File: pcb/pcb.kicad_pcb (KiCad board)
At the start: 2 copper layers, 157.6 x 114.5 mm, 33 parts, among them J1 Conn_01x10, J2 Conn_01x06, J3 Conn_01x06, J4 Conn_01x06, J5 Conn_01x06, J6 Conn_01x06, J7 Conn_01x06, J8 Conn_01x10, U1 teensy-2.0

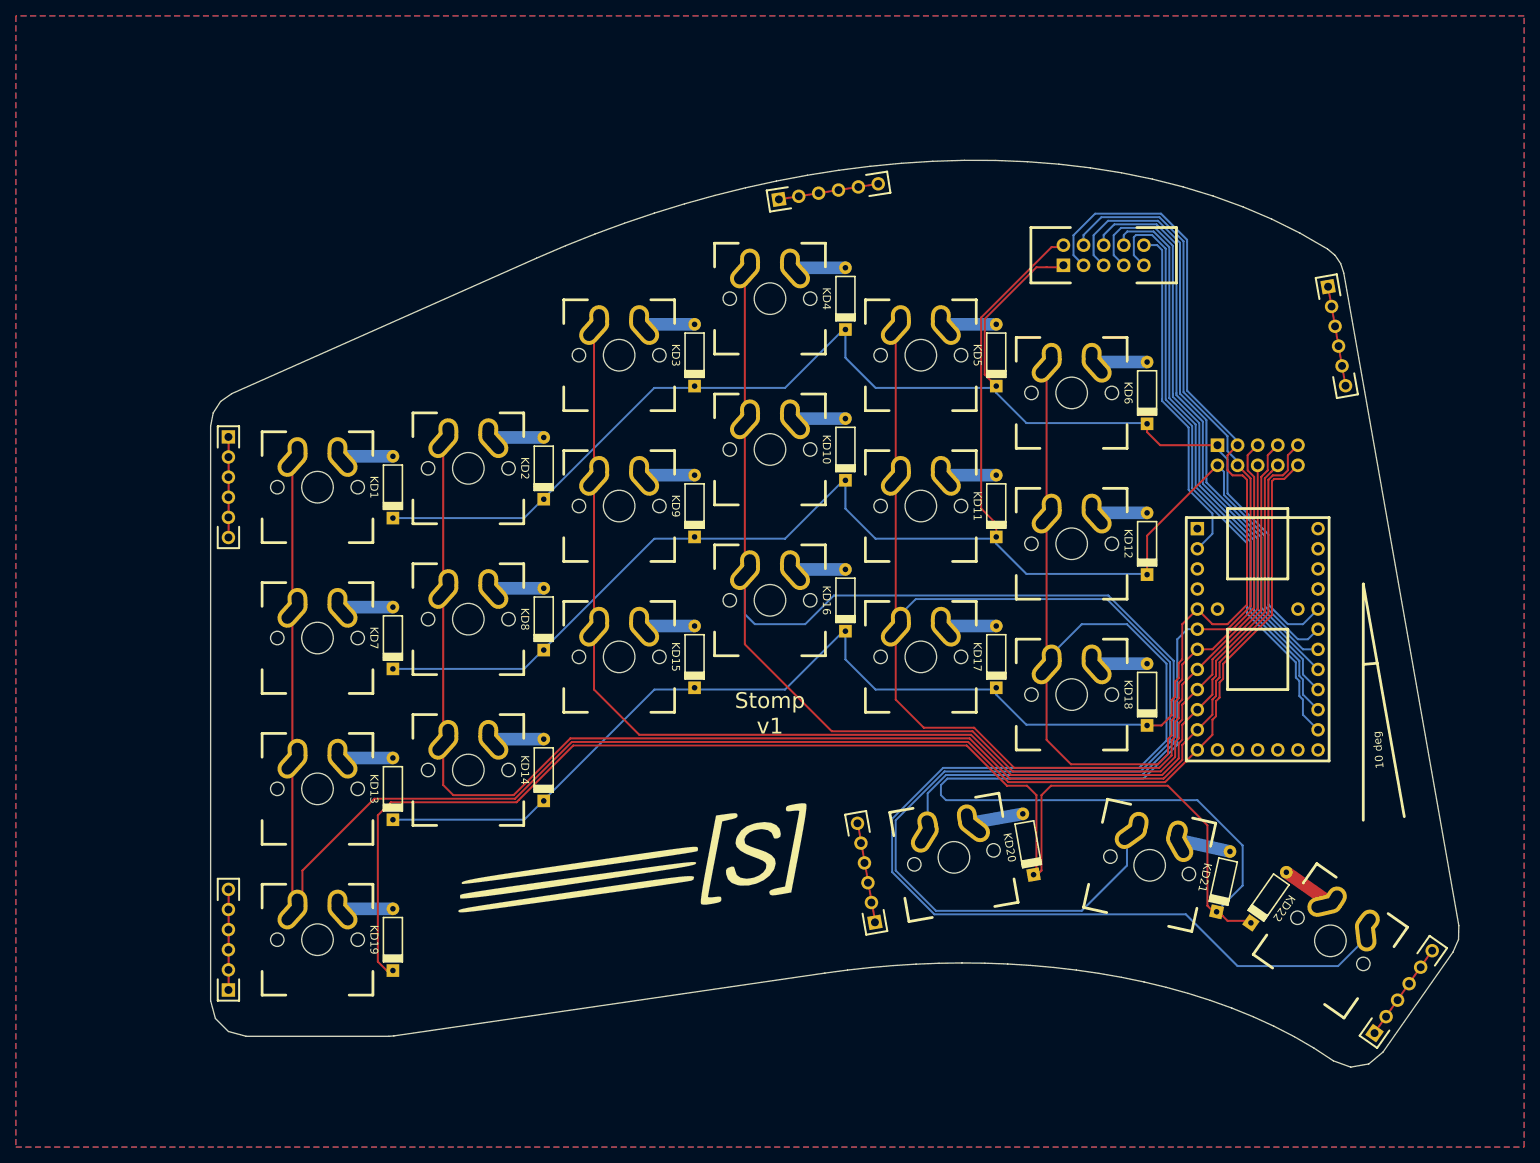
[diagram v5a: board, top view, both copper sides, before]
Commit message: Use single IDC header and prep outline for magnets
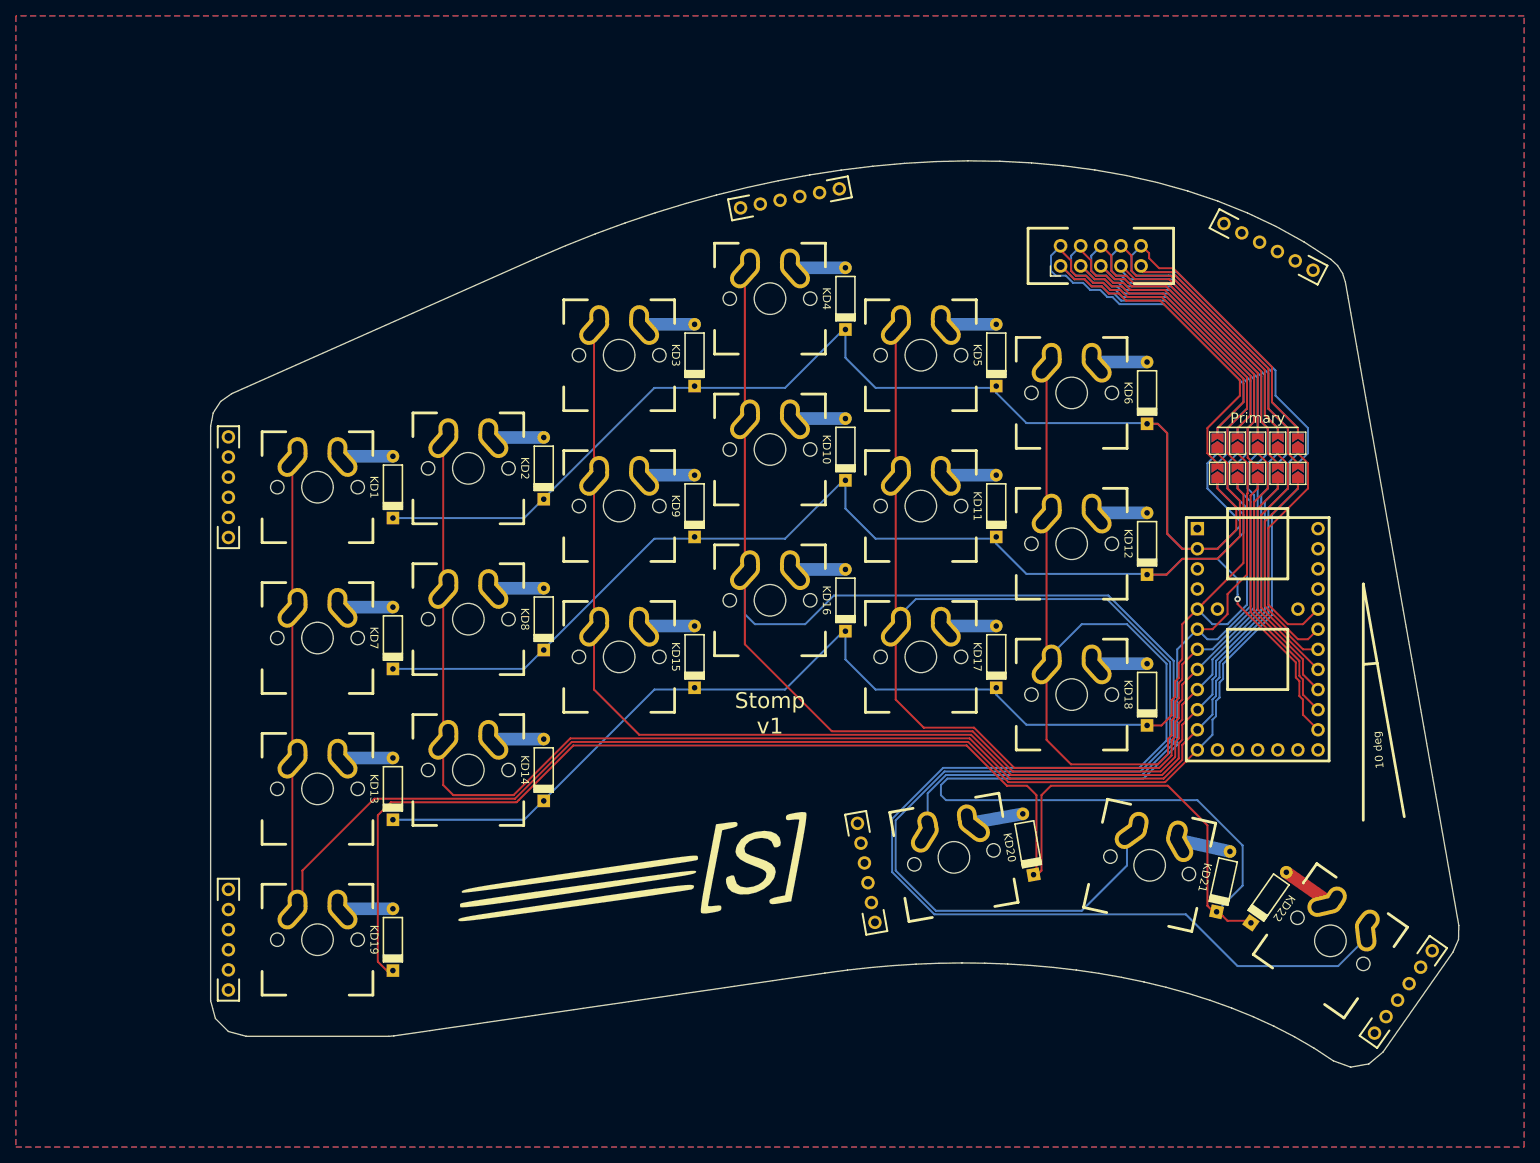
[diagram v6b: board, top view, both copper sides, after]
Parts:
- removed J8: Conn_01x10, keyboard-parts:idc-header_2x05_2.54mm
- added JP1: dualside-idc-jumpers, keyboard-parts:dualside-idc-jumpers, F.Cu at (14.0, -39.4)
- J1: footprint keyboard-parts:idc-header_2x05_2.54mm -> keyboard-parts:idc-header-dualside_2x05_2.54mm
- J2, J3, J4, J5, J6, J7: footprint keyboard-parts:header_1x06_2.54mm -> keyboard-parts:header_sym_1x06_2.54mm
- moved J2 4.96 mm to (-51.3, -71.0), turned to 100.9 degrees
- moved J7 2.82 mm to (21.0, -63.1), turned to 242.4 degrees
- moved G*** 1.11 mm to (-64.8, 13.8) (x2)
- moved J1 0.37 mm to (-5.85, -64.9)
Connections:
- J1 pad 1: /R0 -> Net-(J1-Pad1)
- J1 pad 2: /R1 -> Net-(J1-Pad2)
- J1 pad 3: /R2 -> Net-(J1-Pad3)
- J1 pad 4: /R3 -> Net-(J1-Pad4)
- J2 pad 1: Net-(J2-Pad1) -> GND
- J2 pad 2: Net-(J2-Pad1) -> GND
- J2 pad 3: Net-(J2-Pad1) -> GND
- J2 pad 4: Net-(J2-Pad1) -> GND
- J2 pad 5: Net-(J2-Pad1) -> GND
- J2 pad 6: Net-(J2-Pad1) -> GND
- J3 pad 1: Net-(J3-Pad1) -> GND
- J3 pad 2: Net-(J3-Pad1) -> GND
- J3 pad 3: Net-(J3-Pad1) -> GND
- J3 pad 4: Net-(J3-Pad1) -> GND
- J3 pad 5: Net-(J3-Pad1) -> GND
- J3 pad 6: Net-(J3-Pad1) -> GND
- J4 pad 1: Net-(J4-Pad1) -> GND
- J4 pad 2: Net-(J4-Pad1) -> GND
- J4 pad 3: Net-(J4-Pad1) -> GND
- J4 pad 4: Net-(J4-Pad1) -> GND
- J4 pad 5: Net-(J4-Pad1) -> GND
- J4 pad 6: Net-(J4-Pad1) -> GND
- J5 pad 1: Net-(J5-Pad1) -> GND
- J5 pad 2: Net-(J5-Pad1) -> GND
- J5 pad 3: Net-(J5-Pad1) -> GND
- J5 pad 4: Net-(J5-Pad1) -> GND
- J5 pad 5: Net-(J5-Pad1) -> GND
- J5 pad 6: Net-(J5-Pad1) -> GND
- J6 pad 1: Net-(J6-Pad1) -> GND
- J6 pad 2: Net-(J6-Pad1) -> GND
- J6 pad 3: Net-(J6-Pad1) -> GND
- J6 pad 4: Net-(J6-Pad1) -> GND
- J6 pad 5: Net-(J6-Pad1) -> GND
- J6 pad 6: Net-(J6-Pad1) -> GND
- J7 pad 1: Net-(J7-Pad1) -> GND
- J7 pad 2: Net-(J7-Pad1) -> GND
- J7 pad 3: Net-(J7-Pad1) -> GND
- J7 pad 4: Net-(J7-Pad1) -> GND
- J7 pad 5: Net-(J7-Pad1) -> GND
- J7 pad 6: Net-(J7-Pad1) -> GND
- U1 pad 19: Net-(J1-Pad9) -> /R1
- U1 pad 2: Net-(J1-Pad10) -> /R0
- U1 pad 20: Net-(J1-Pad8) -> Net-(JP1-Pad5)
- U1 pad 21: Net-(J1-Pad7) -> Net-(JP1-Pad6)
- U1 pad 22: Net-(J1-Pad6) -> Net-(JP1-Pad7)
- U1 pad 23: Net-(J1-Pad5) -> Net-(JP1-Pad8)
- U1 pad 24: /R1 -> Net-(JP1-Pad9)
- U1 pad 25: /R0 -> Net-(JP1-Pad10)
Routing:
- net Net-(J1-Pad1): track 0.00 -> 84.1 mm
- net Net-(J1-Pad2): track 0.00 -> 81.3 mm
- net Net-(J1-Pad3): track 0.00 -> 79.9 mm
- net Net-(J1-Pad4): track 0.00 -> 77.1 mm
- net Net-(JP1-Pad6): track 0.00 -> 35.1 mm
- net Net-(JP1-Pad5): track 0.00 -> 33.1 mm
- net /R2: track 211.8 -> 180.1 mm
- net Net-(JP1-Pad8): track 0.00 -> 31.3 mm
- net Net-(JP1-Pad10): track 0.00 -> 30.4 mm
- net Net-(JP1-Pad7): track 0.00 -> 28.3 mm
- net Net-(JP1-Pad9): track 0.00 -> 26.8 mm
- net Net-(J1-Pad10): track 43.7 -> 69.6 mm
- net /R3: track 343.0 -> 322.0 mm
- net /R1: track 201.7 -> 188.6 mm, vias 0 -> 1
- net Net-(J7-Pad1): track 12.7 -> 0.00 mm
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- added copper zone on B.Cu, net GND
- added copper zone on F.Cu, net GND
- removed copper zone on B.Cu, net (none)
- removed copper zone on F.Cu, net (none)
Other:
- outline, holes or cut-outs redrawn

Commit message: Add higher resolution outline curves and magnet supports
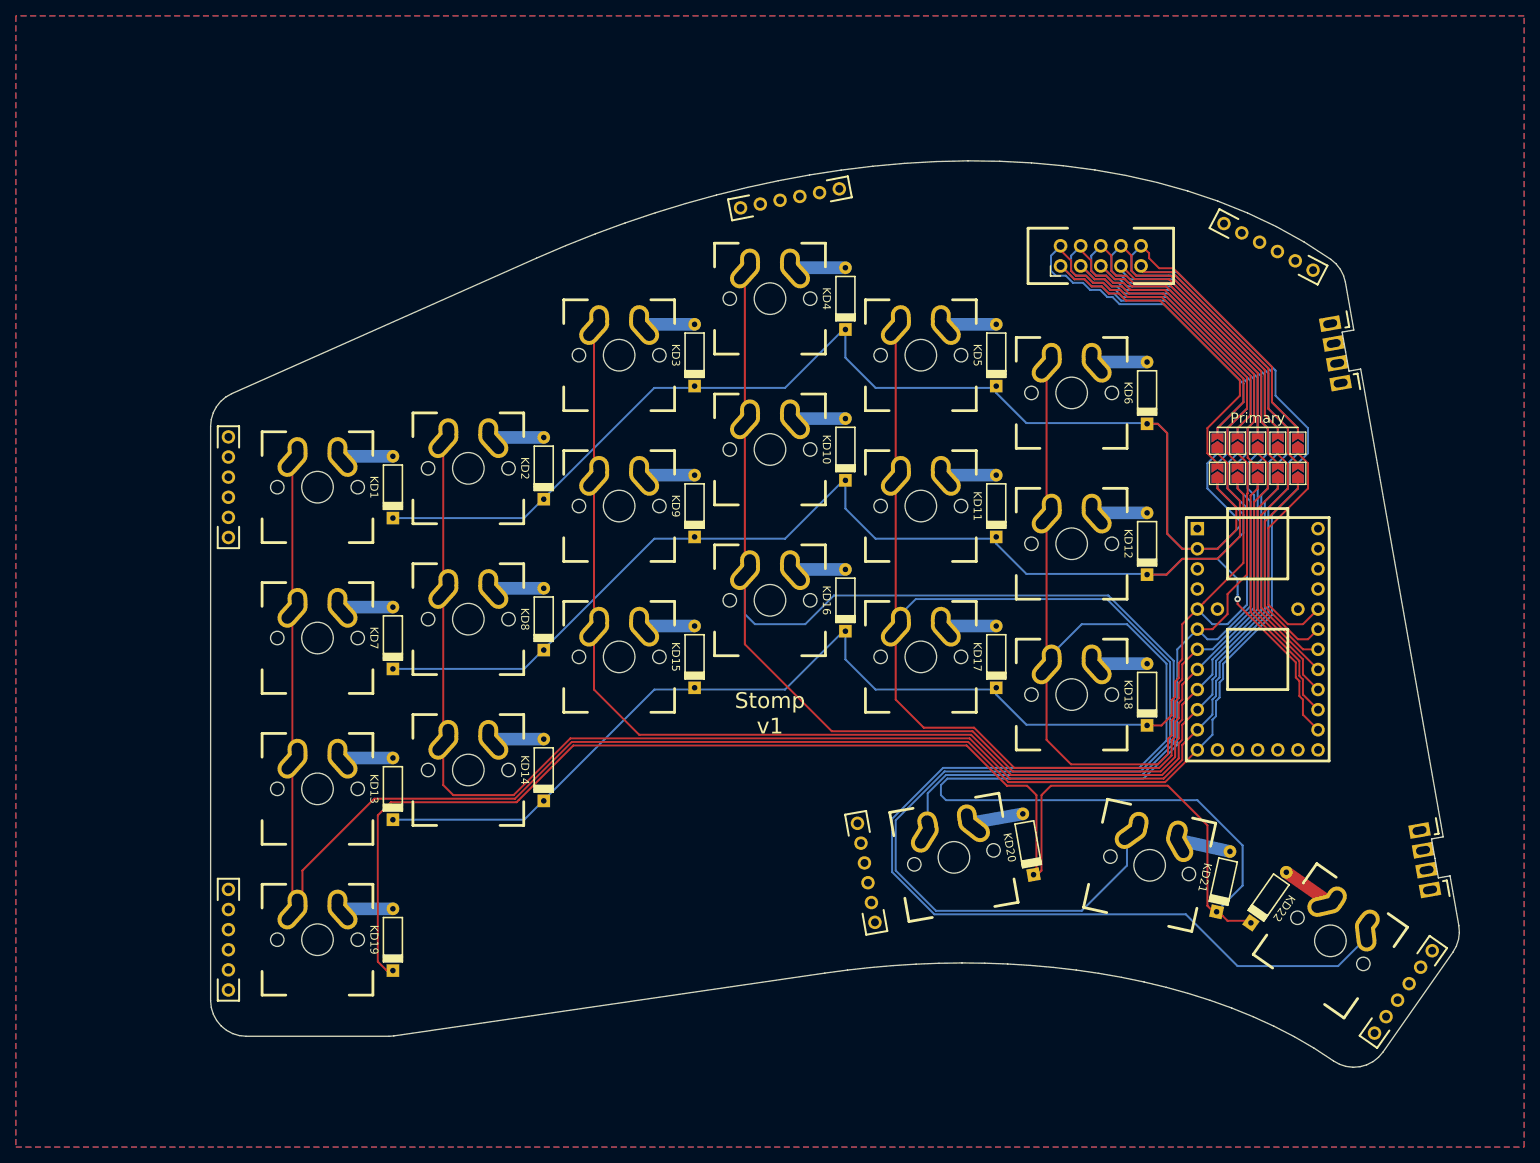
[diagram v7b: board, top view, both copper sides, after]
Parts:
- removed G***: LOGO, logos:smark-rev
- removed G***: LOGO, logos:smark
- added REF**: magnet-support, keyboard-parts:magnet-support, F.Cu at (37.8, 10.9)
- added REF**: magnet-support, keyboard-parts:magnet-support, F.Cu at (26.5, -53.1)
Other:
- board size 157.6 x 114.5 mm -> 157.7 x 114.5 mm
- board text removed: "10 deg"

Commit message: Update version number to v2 and add new gerbers
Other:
- board text added: "Stomp v2"
- board text removed: "Stomp v1"
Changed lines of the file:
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@@
     (visible_elements 7EFFF7FF)
     (pcbplotparams
-      (layerselection 0x00e00_7ffffffe)
+      (layerselection 0x010fc_ffffffff)
       (usegerberextensions true)
       (usegerberattributes false)
@@
       (padsonsilk false)
       (subtractmaskfromsilk false)
-      (outputformat 3)
+      (outputformat 1)
       (mirror false)
       (drillshape 0)
       (scaleselection 1)
-      (outputdirectory "../plate/outlines/"))
+      (outputdirectory "../gerbers/"))
   )
   (net 0 "")
@@
     (effects (font (size 2 2) (thickness 0.3)) (justify mirror))
   )
-  (gr_text "Stomp\nv1" (at -47.625 -7.14375) (layer F.SilkS)
+  (gr_text "Stomp\nv2" (at -47.625 -7.14375) (layer F.SilkS)
     (effects (font (size 2 2) (thickness 0.3)))
   )
